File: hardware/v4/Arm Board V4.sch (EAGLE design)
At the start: 42 parts, among them IC7 7812DT, IC9 7812DT, Q1 MOSFET-NCHANNELFQP30N06L, Q2 MOSFET-NCHANNELFQP30N06L, Q3 Q_LTC490, Q4 MOSFET-NCHANNELFQP30N06L, U1 SN74LS241DW, U2 XBEE-1B3

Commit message: A lot of updates getting close to a final board
Did a lot of changes that got the board closer to the final version.
Skipped a lot of commits because who cares and github was not getting
along with me.
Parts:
- removed C20, C21, C22, C23: .1uF, SparkFun-Capacitors:2.2UF-CERCAP-10009
- removed IC7, IC9: 7812DT, linear:7812DT
- removed JP1, JP2: M025MM, SparkFun-Connectors:M025MM
- removed JP13: (no value), SparkFun-Connectors:M03POLAR
- removed JP5: (no value), SparkFun-Connectors:M041X04_NO_SILK
- removed Q1, Q2, Q4: MOSFET-NCHANNELFQP30N06L, SparkFun-DiscreteSemi:MOSFET-NCHANNELFQP30N06L
- removed Q3: Q_LTC490, PCB0M1:Q_LTC490
- added C1: .1uF, SparkFun-Capacitors:CAP1206
- added C3: (no value), SparkFun-Passives:CAP_POLC
- added C5: .22uF, SparkFun-Capacitors:CAP1206
- added C6: 4.7uF, SparkFun-Capacitors:CAP1206
- added C7: 1uF, SparkFun-Capacitors:CAP1206
- added C8: 10uF, SparkFun-Capacitors:10UF-16V-10%(TANT)
- added IC2: REG1118, burr-brown:REG1118
- added JP3: M025MM, SparkFun-Connectors:M025MM
- added LED5: RED, SparkFun-LED:LED-RED0603
- added R1: 16.5k, SparkFun-Passives:RESISTOR1206
- added R2, R4, R5: 10k, SparkFun-Resistors:RESISTOR1206
- added R9: 1k, SparkFun-Passives:RESISTOR1206
- added U$4: MAX3077, MAX3077:MAX3077
- added U3: LSM9DS0, SparkFun-DigitalIC:LSM9DS0
- C12: device SparkFun-Capacitors:2.2UF-CERCAP-10009 -> SparkFun-Capacitors:CAP1206
- JP4: device SparkFun-Connectors:M041X04_NO_SILK -> SparkFun-Connectors:M04SCREW
- LED1, LED2: value Red -> RED
- LED3: value Green -> GREEN
- R12, R13, R14: device SparkFun-Resistors:1KOHM1/10W1%(0603) -> SparkFun-Passives:RESISTOR1206
- R3, R6, R7: value 150 -> 10k; device SparkFun-Passives:RESISTOR1206 -> SparkFun-Resistors:RESISTOR1206
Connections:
- removed net 5VIN: JP7.2
- removed net O1: JP4.2, JP5.2, Q1.D
- removed net O2: JP4.3, JP5.3, Q2.D
- removed net O3: JP4.4, JP5.4, Q4.D
- new net +3.3V: IC2.VOUT, R12.2, R13.1, R14.1, U2.VDD
- new net CS_G: R4.1, U3.CS(G)
- new net CS_XM: R5.1, U3.CS(XM)
- new net DEN_G: U3.DEN(G)
- new net DRDY_G: U3.DRDY(G)
- new net INT1_XM: U3.INT1(XM)
- new net INT2_XM: U3.INT2(XM)
- new net INT_G: U3.INT(G)
- new net N$10: C5.1, U3.SETP
- new net N$11: C5.2, U3.SETC
- new net N$12: C6.1, U3.C1
- new net N$14: LED5.A, R9.1
- new net N$9: R1.2, U$2.ADJUST
- new net SCL: R3.1, U$1.PA6, U3.SCL
- new net SDA: R2.1, U$1.PA7, U3.SDA
- new net SDO_G: R7.1, U3.SDO(G)
- new net SDO_XM: R6.1, U3.SDO(XM)
- net +12V: now also JP3.1, JP4.3; no longer C20.1, C22.1, IC7.VI, IC9.VI, JP1.1, JP13.2, JP4.1, JP5.1
- net +3V3: now also C7.1, C8.+, R2.2, R3.2, R4.2, R5.2, R6.2, R7.2, U3.VDD, U3.VDD_IO; no longer C12.1, C23.1, IC9.VO, Q3.VCC, R12.2, R13.1, R14.1, U2.VDD
- net +5V: now also C12.1, IC2.VIN, JP4.4, JP7.2, U$1.VBUS, U$4.VCC; no longer C21.1, IC7.VO
- net 14.8V: now also C3.+
- net DDATA_1: no longer JP13.3
- net GND: now also C1.2, C3.-, C6.2, C7.2, C8.-, IC2.GND, JP3.2, JP4.1, LED5.C, R1.1, U$4.GND, U3.GND; no longer C20.2, C21.2, C22.2, C23.2, IC7.GND, IC9.GND, JP1.2, JP13.1, JP2.2, Q1.S, Q2.S, Q3.GND, Q4.S, R3.1, R6.1, R7.1
- net N$1: now also U$4.Z; no longer Q3.Z
- net N$2: now also U$4.B; no longer Q3.B
- net N$3: now also U$4.A; no longer Q3.A
- net N$5: now also U$4.Y; no longer Q3.Y
- net PWM1: no longer Q1.G, R3.2
- net PWM2: no longer Q2.G, R6.2
- net PWM3: no longer Q4.G, R7.2
- net RX_2: now also U$4.R0; no longer Q3.R
- net TX_2: now also U$4.DI; no longer Q3.D
- net VIN: now also C1.1, JP4.2, R9.2; no longer JP2.1
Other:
- note added: "0 1"
- note added: "0x1E 0x1D"
- note added: "0x6A 0x6B"
- note added: "Close these jumpers to hard-set I2C mode. Gyro Address = 0x6B Accel/Mag Address = 0x1D"
- note added: "G Addr."
- note added: "Jim Lindblom"
- note added: "SDA/SCL Pull-up resistors"
- note added: "SDOG/XM"
- note added: "Set the SDO_G and SDO_XM to set the gyro and accel/mag I2C addresses:"
- note added: "XM Addr."
- note added: "v10"

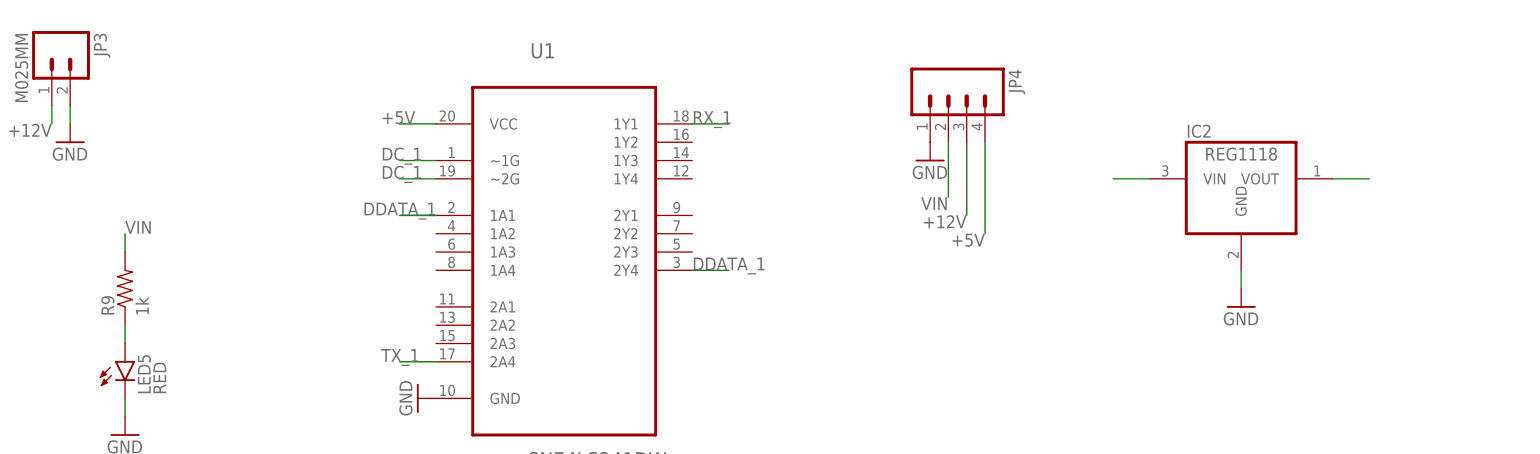
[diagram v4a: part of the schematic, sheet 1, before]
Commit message: Added a few capacitors
Added capacitors on voltage supplies and regulator.
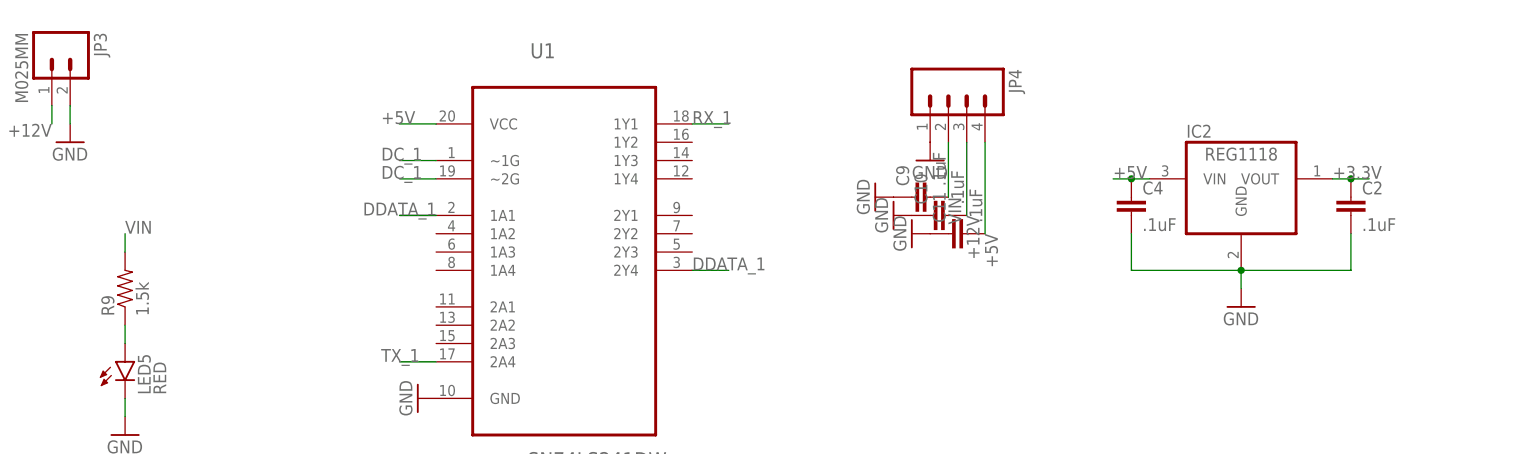
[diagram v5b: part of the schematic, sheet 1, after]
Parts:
- added C10, C11, C2, C4, C9: .1uF, SparkFun-Capacitors:CAP1206
- R9: value 1k -> 1.5k
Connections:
- net +12V: now also C10.2
- net +3.3V: now also C2.1
- net +5V: now also C11.2, C4.1
- net GND: now also C10.1, C11.1, C2.2, C4.2, C9.1
- net VIN: now also C9.2
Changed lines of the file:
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@@
 <?xml version="1.0" encoding="utf-8"?>
 <!DOCTYPE eagle SYSTEM "eagle.dtd">
-<eagle version="7.1.0">
+<eagle version="6.5.0">
 <drawing>
 <settings>
@@
 <part name="R6" library="SparkFun-Resistors" deviceset="RESISTOR" device="1206" value="10k"/>
 <part name="R7" library="SparkFun-Resistors" deviceset="RESISTOR" device="1206" value="10k"/>
-<part name="R9" library="SparkFun-Passives" deviceset="RESISTOR" device="1206" value="1k"/>
+<part name="R9" library="SparkFun-Passives" deviceset="RESISTOR" device="1206" value="1.5k"/>
 <part name="LED5" library="SparkFun-LED" deviceset="LED-RED" device="0603" value="RED"/>
 <part name="GND30" library="SparkFun" deviceset="GND" device=""/>
@@
 <part name="GND17" library="SparkFun-Aesthetics" deviceset="GND" device=""/>
 <part name="IC2" library="burr-brown" deviceset="REG1118" device=""/>
+<part name="C2" library="SparkFun-Capacitors" deviceset="CAP" device="1206" value=".1uF"/>
+<part name="C4" library="SparkFun-Capacitors" deviceset="CAP" device="1206" value=".1uF"/>
+<part name="C9" library="SparkFun-Capacitors" deviceset="CAP" device="1206" value=".1uF"/>
+<part name="C10" library="SparkFun-Capacitors" deviceset="CAP" device="1206" value=".1uF"/>
+<part name="C11" library="SparkFun-Capacitors" deviceset="CAP" device="1206" value=".1uF"/>
+<part name="GND22" library="SparkFun-Aesthetics" deviceset="GND" device=""/>
+<part name="GND24" library="SparkFun-Aesthetics" deviceset="GND" device=""/>
+<part name="GND29" library="SparkFun-Aesthetics" deviceset="GND" device=""/>
 </parts>
 <sheets>
@@
 <instance part="GND17" gate="1" x="170.18" y="-17.78"/>
 <instance part="IC2" gate="G$1" x="170.18" y="0"/>
+<instance part="C2" gate="G$1" x="185.42" y="-5.08"/>
+<instance part="C4" gate="G$1" x="154.94" y="-5.08"/>
+<instance part="C9" gate="G$1" x="127" y="-2.54" rot="R90"/>
+<instance part="C10" gate="G$1" x="129.54" y="-5.08" rot="R90"/>
+<instance part="C11" gate="G$1" x="132.08" y="-7.62" rot="R90"/>
+<instance part="GND22" gate="1" x="119.38" y="-2.54" rot="R270"/>
+<instance part="GND24" gate="1" x="121.92" y="-5.08" rot="R270"/>
+<instance part="GND29" gate="1" x="124.46" y="-7.62" rot="R270"/>
 </instances>
 <busses>
@@
 <pinref part="GND17" gate="1" pin="GND"/>
 <wire x1="170.18" y1="-15.24" x2="170.18" y2="-12.7" width="0.1524" layer="91"/>
+<pinref part="C4" gate="G$1" pin="2"/>
+<wire x1="154.94" y1="-7.62" x2="154.94" y2="-12.7" width="0.1524" layer="91"/>
+<wire x1="154.94" y1="-12.7" x2="170.18" y2="-12.7" width="0.1524" layer="91"/>
+<pinref part="C2" gate="G$1" pin="2"/>
+<wire x1="185.42" y1="-7.62" x2="185.42" y2="-12.7" width="0.1524" layer="91"/>
+<wire x1="185.42" y1="-12.7" x2="170.18" y2="-12.7" width="0.1524" layer="91"/>
+<junction x="170.18" y="-12.7"/>
+</segment>
+<segment>
+<pinref part="C9" gate="G$1" pin="1"/>
+<pinref part="GND22" gate="1" pin="GND"/>
+</segment>
+<segment>
+<pinref part="C10" gate="G$1" pin="1"/>
+<pinref part="GND24" gate="1" pin="GND"/>
+</segment>
+<segment>
+<pinref part="C11" gate="G$1" pin="1"/>
+<pinref part="GND29" gate="1" pin="GND"/>
 </segment>
 </net>
@@
 <pinref part="JP4" gate="G$1" pin="3"/>
 <wire x1="132.08" y1="5.08" x2="132.08" y2="-5.08" width="0.1524" layer="91"/>
-<label x="132.08" y="-5.08" size="1.778" layer="95" rot="R180"/>
+<label x="132.08" y="-5.08" size="1.778" layer="95" rot="R270"/>
+<pinref part="C10" gate="G$1" pin="2"/>
 </segment>
 </net>
@@
 <pinref part="JP4" gate="G$1" pin="4"/>
 <wire x1="134.62" y1="5.08" x2="134.62" y2="-7.62" width="0.1524" layer="91"/>
-<label x="134.62" y="-7.62" size="1.778" layer="95" rot="R180"/>
-</segment>
-<segment>
-<wire x1="152.4" y1="0" x2="157.48" y2="0" width="0.1524" layer="91"/>
+<label x="134.62" y="-7.62" size="1.778" layer="95" rot="R270"/>
+<pinref part="C11" gate="G$1" pin="2"/>
+</segment>
+<segment>
+<wire x1="152.4" y1="0" x2="154.94" y2="0" width="0.1524" layer="91"/>
 <pinref part="IC2" gate="G$1" pin="VIN"/>
+<label x="152.4" y="0" size="1.778" layer="95"/>
+<pinref part="C4" gate="G$1" pin="1"/>
+<wire x1="154.94" y1="0" x2="157.48" y2="0" width="0.1524" layer="91"/>
+<junction x="154.94" y="0"/>
 </segment>
 </net>
@@
 <pinref part="JP4" gate="G$1" pin="2"/>
 <wire x1="129.54" y1="5.08" x2="129.54" y2="-2.54" width="0.1524" layer="91"/>
-<label x="129.54" y="-2.54" size="1.778" layer="95" rot="R180"/>
+<label x="129.54" y="-2.54" size="1.778" layer="95" rot="R270"/>
+<pinref part="C9" gate="G$1" pin="2"/>
 </segment>
 </net>
@@
 <net name="+3.3V" class="0">
 <segment>
-<wire x1="182.88" y1="0" x2="187.96" y2="0" width="0.1524" layer="91"/>
+<wire x1="182.88" y1="0" x2="185.42" y2="0" width="0.1524" layer="91"/>
 <pinref part="IC2" gate="G$1" pin="VOUT"/>
-</segment>
-</net>
+<label x="182.88" y="0" size="1.778" layer="95"/>
+<pinref part="C2" gate="G$1" pin="1"/>
+<wire x1="185.42" y1="0" x2="187.96" y2="0" width="0.1524" layer="91"/>
+<junction x="185.42" y="0"/>
+</segment>
+</net>
